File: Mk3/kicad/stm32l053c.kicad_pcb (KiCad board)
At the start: 2 copper layers, 26.7 x 43.2 mm, 34 parts, among them J1 LGT, J2 GND, J3 TX, J4 A0, J5 A1, J6 A3, J7 A2, P1 SWD, U1 AP2112, U2 STM32L053C8_LQFP48, U3 ADS1015, U4 UFL_SMA, U5 RFM92/95

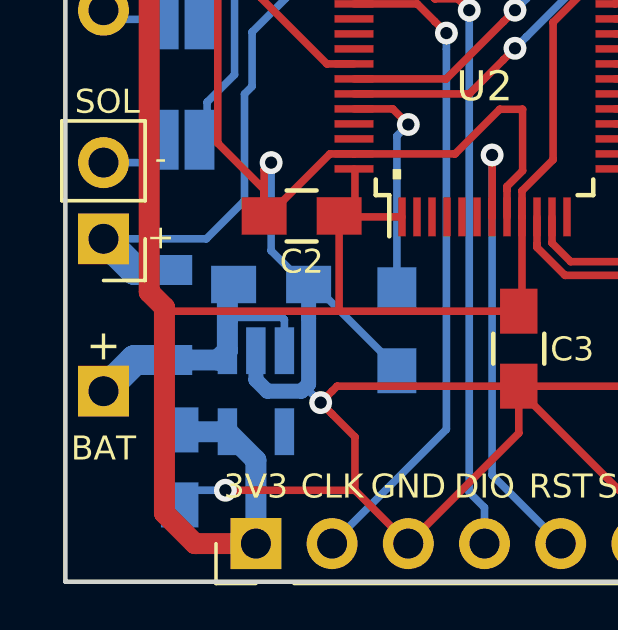
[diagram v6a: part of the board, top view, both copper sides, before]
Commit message: Diode SOD-323
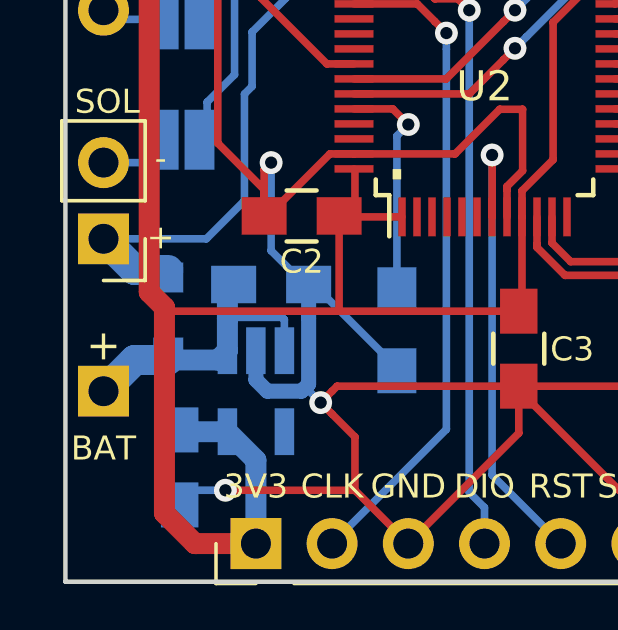
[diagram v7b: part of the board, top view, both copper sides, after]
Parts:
- D2: footprint Diodes_SMD:D_1206 -> Diodes_SMD:D_SOD-323_HandSoldering
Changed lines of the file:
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@@
     )
-  )
-  (module Diodes_SMD:D_1206 (layer B.Cu)
-    (at 139.319 86.36 90)
-    (descr "Diode SMD 1206, reflow soldering")
-    (tags "Diode 1206")
-    (attr smd)
-    (fp_text reference D2 (at 0 2.3 90) (layer B.SilkS)
-      (effects (font (size 1 1) (thickness 0.15)) (justify mirror))
-    )
-    (fp_text value D_Schottky (at 0 -2.3 90) (layer B.Fab)
-      (effects (font (size 1 1) (thickness 0.15)) (justify mirror))
-    )
-    (fp_line (start -0.254 0.254) (end -0.254 -0.254) (layer B.Fab) (width 0.1))
-    (fp_line (start 0.127 0) (end 0.381 0) (layer B.Fab) (width 0.1))
-    (fp_line (start -0.254 0) (end -0.508 0) (layer B.Fab) (width 0.1))
-    (fp_line (start 0.127 -0.254) (end -0.254 0) (layer B.Fab) (width 0.1))
-    (fp_line (start 0.127 0.254) (end 0.127 -0.254) (layer B.Fab) (width 0.1))
-    (fp_line (start -0.254 0) (end 0.127 0.254) (layer B.Fab) (width 0.1))
-    (fp_line (start -2.2 1.016) (end -2.2 -1.016) (layer B.SilkS) (width 0.12))
-    (fp_line (start -1.6 -0.8) (end -1.6 0.8) (layer B.Fab) (width 0.1))
-    (fp_line (start 1.6 -0.8) (end -1.6 -0.8) (layer B.Fab) (width 0.1))
-    (fp_line (start 1.6 0.8) (end 1.6 -0.8) (layer B.Fab) (width 0.1))
-    (fp_line (start -1.6 0.8) (end 1.6 0.8) (layer B.Fab) (width 0.1))
-    (fp_line (start -2.3 1.15) (end 2.3 1.15) (layer B.CrtYd) (width 0.05))
-    (fp_line (start -2.3 -1.15) (end 2.3 -1.15) (layer B.CrtYd) (width 0.05))
-    (fp_line (start -2.3 1.15) (end -2.3 -1.15) (layer B.CrtYd) (width 0.05))
-    (fp_line (start 2.3 1.15) (end 2.3 -1.15) (layer B.CrtYd) (width 0.05))
-    (fp_line (start 1 1.025) (end -2.2 1.025) (layer B.SilkS) (width 0.12))
-    (fp_line (start -2.2 -1.025) (end 1 -1.025) (layer B.SilkS) (width 0.12))
-    (pad 1 smd rect (at -1.5 0 90) (size 1 1.6) (layers B.Cu B.Paste B.Mask)
-      (net 32 "Net-(BT1-Pad1)"))
-    (pad 2 smd rect (at 1.5 0 90) (size 1 1.6) (layers B.Cu B.Paste B.Mask)
-      (net 33 "Net-(D2-Pad2)"))
   )
   (module Pin_Headers:Pin_Header_Straight_1x01_Pitch2.54mm (layer F.Cu)
@@
     )
   )
+  (module Diodes_SMD:D_SOD-323_HandSoldering (layer B.Cu)
+    (at 139.319 86.36 90)
+    (descr SOD-323)
+    (tags SOD-323)
+    (attr smd)
+    (fp_text reference D2 (at 0 1.85 90) (layer B.SilkS)
+      (effects (font (size 1 1) (thickness 0.15)) (justify mirror))
+    )
+    (fp_text value D_Schottky (at 0.1 -1.9 90) (layer B.Fab)
+      (effects (font (size 1 1) (thickness 0.15)) (justify mirror))
+    )
+    (fp_line (start -1.9 0.85) (end -1.9 -0.85) (layer B.SilkS) (width 0.12))
+    (fp_line (start 0.2 0) (end 0.45 0) (layer B.Fab) (width 0.1))
+    (fp_line (start 0.2 -0.35) (end -0.3 0) (layer B.Fab) (width 0.1))
+    (fp_line (start 0.2 0.35) (end 0.2 -0.35) (layer B.Fab) (width 0.1))
+    (fp_line (start -0.3 0) (end 0.2 0.35) (layer B.Fab) (width 0.1))
+    (fp_line (start -0.3 0) (end -0.5 0) (layer B.Fab) (width 0.1))
+    (fp_line (start -0.3 0.35) (end -0.3 -0.35) (layer B.Fab) (width 0.1))
+    (fp_line (start -0.9 -0.7) (end -0.9 0.7) (layer B.Fab) (width 0.1))
+    (fp_line (start 0.9 -0.7) (end -0.9 -0.7) (layer B.Fab) (width 0.1))
+    (fp_line (start 0.9 0.7) (end 0.9 -0.7) (layer B.Fab) (width 0.1))
+    (fp_line (start -0.9 0.7) (end 0.9 0.7) (layer B.Fab) (width 0.1))
+    (fp_line (start -2 0.95) (end 2 0.95) (layer B.CrtYd) (width 0.05))
+    (fp_line (start 2 0.95) (end 2 -0.95) (layer B.CrtYd) (width 0.05))
+    (fp_line (start -2 -0.95) (end 2 -0.95) (layer B.CrtYd) (width 0.05))
+    (fp_line (start -2 0.95) (end -2 -0.95) (layer B.CrtYd) (width 0.05))
+    (fp_line (start -1.9 -0.85) (end 1.25 -0.85) (layer B.SilkS) (width 0.12))
+    (fp_line (start -1.9 0.85) (end 1.25 0.85) (layer B.SilkS) (width 0.12))
+    (pad 1 smd rect (at -1.25 0 90) (size 1 1) (layers B.Cu B.Paste B.Mask)
+      (net 32 "Net-(BT1-Pad1)"))
+    (pad 2 smd rect (at 1.25 0 90) (size 1 1) (layers B.Cu B.Paste B.Mask)
+      (net 33 "Net-(D2-Pad2)"))
+    (model Diodes_SMD.3dshapes/D_SOD-323.wrl
+      (at (xyz 0 0 0))
+      (scale (xyz 1 1 1))
+      (rotate (xyz 0 0 180))
+    )
+  )

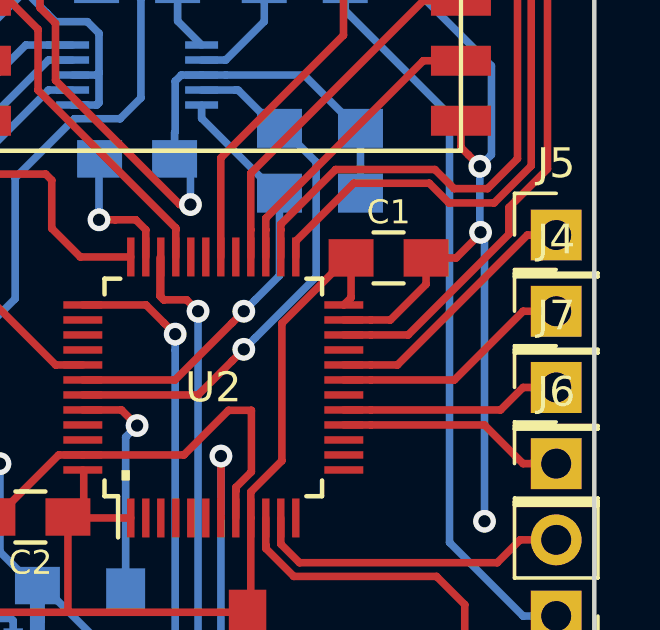
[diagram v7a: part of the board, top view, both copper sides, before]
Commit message: Corrected analog pin connections
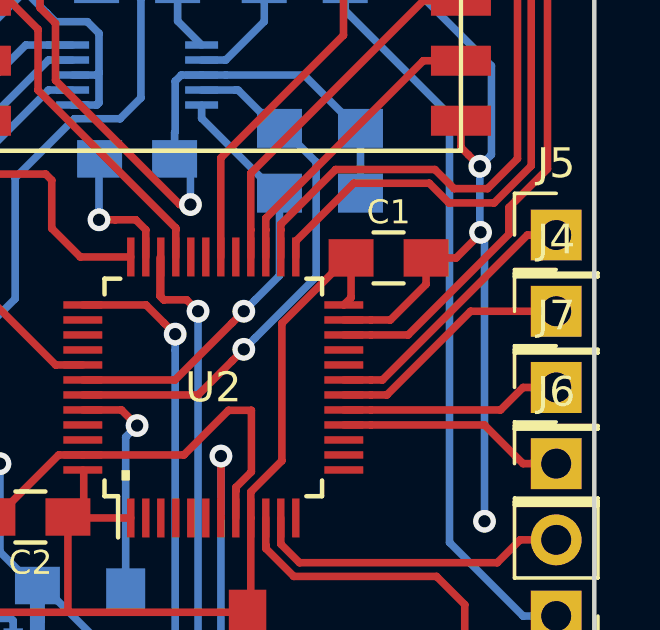
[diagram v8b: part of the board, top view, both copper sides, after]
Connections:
- U2 pad 18: Net-(U2-Pad18) -> Net-(J4-Pad1)
- U2 pad 19: Net-(J4-Pad1) -> Net-(J5-Pad1)
- U2 pad 20: Net-(J5-Pad1) -> Net-(U2-Pad20)
